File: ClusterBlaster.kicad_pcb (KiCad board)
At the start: 2 copper layers, 12 parts, among them J1 Conn_01x04, U1 LM339, U2 L7805

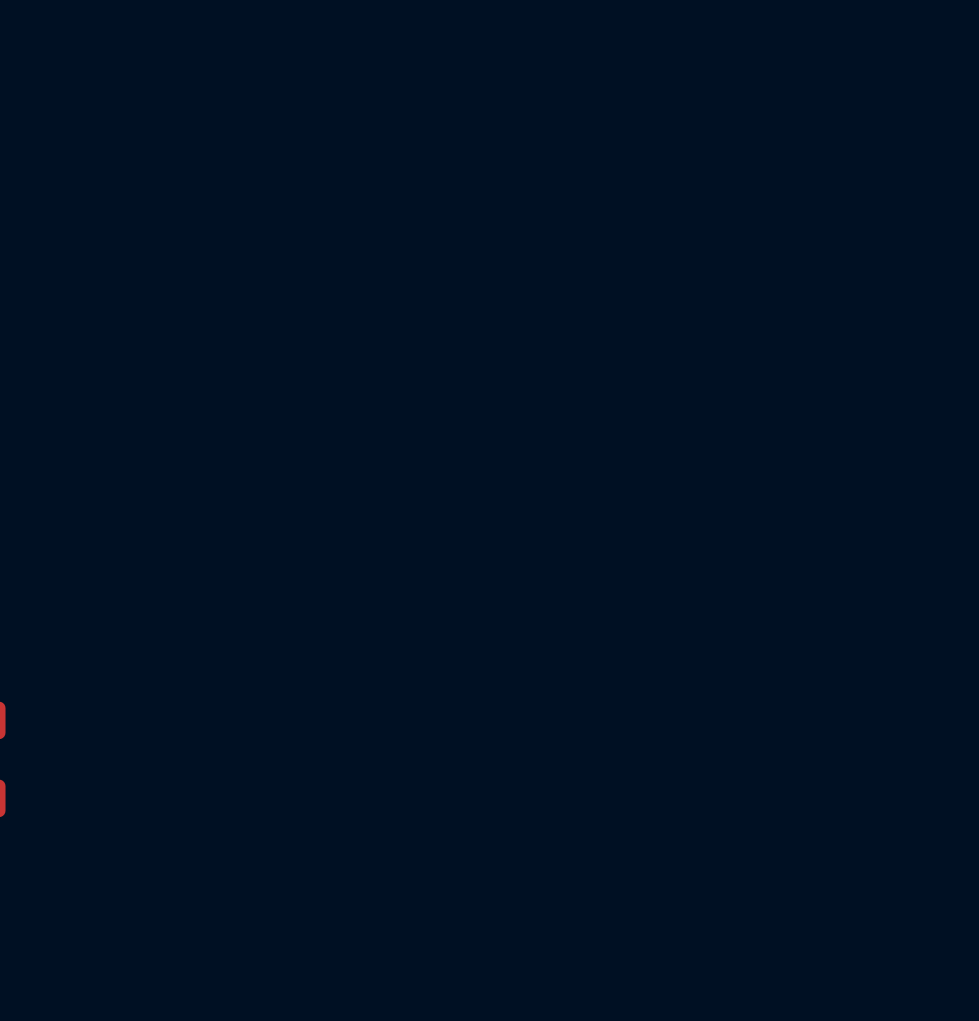
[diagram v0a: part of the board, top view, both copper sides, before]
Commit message: Added Arduino symbol and footprint
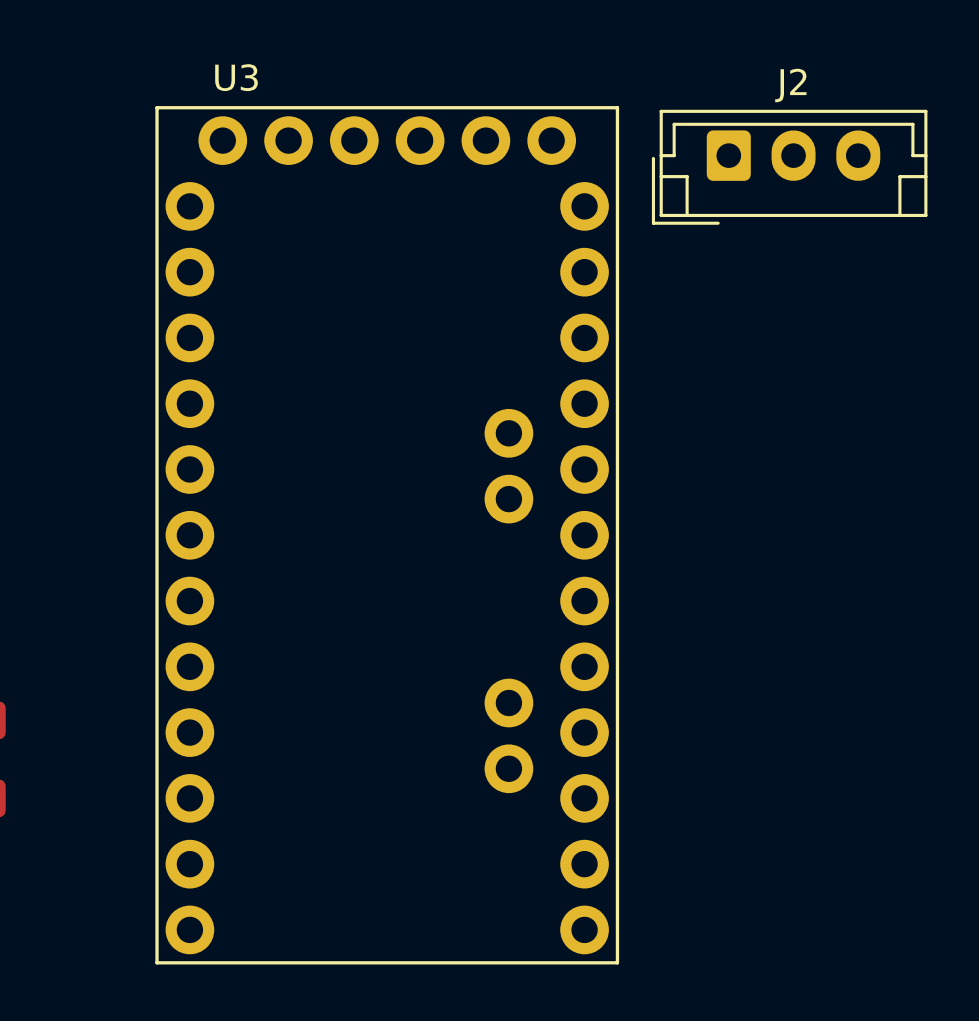
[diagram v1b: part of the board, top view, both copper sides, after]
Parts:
- added J2: Conn_01x03, Connector_JST:JST_EH_B3B-EH-A_1x03_P2.50mm_Vertical, F.Cu at (165.6, 56.5)
- added U3: ARDUINO_PRO_MINI, Pro_Mini:MODULE_ARDUINO_PRO_MINI, F.Cu at (152.4, 71.1)

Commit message: Added all the components
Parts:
- added R10: 10k, Resistor_SMD:R_0805_2012Metric, F.Cu at (175.1, 69.1)
- added R8: 10k, Resistor_SMD:R_0805_2012Metric, F.Cu at (175.1, 63.2)
- added R9: 10k, Resistor_SMD:R_0805_2012Metric, F.Cu at (175.1, 66.2)
- added SW1: SW_Push, Button_Switch_THT:SW_PUSH_6mm, F.Cu at (164.4, 63.8)
- added SW2: SW_Push, Button_Switch_THT:SW_PUSH_6mm, F.Cu at (164.4, 72.3)
- added SW3: SW_Push, Button_Switch_THT:SW_PUSH_6mm, F.Cu at (164.4, 80.9)
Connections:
- U3 pad JP1_4: unconnected-(U3-VCC-PadJP1_4) -> 5V
- U3 pad JP1_5: Net-(U3-GND-PadJP1_5) -> GND
- U3 pad JP1_6: Net-(U3-GND-PadJP1_5) -> GND
- U3 pad JP6_2: unconnected-(U3-GND_1-PadJP6_2) -> GND
- U3 pad JP6_4: unconnected-(U3-VCC_1-PadJP6_4) -> 5V
- U3 pad JP7_1: unconnected-(U3-D9-PadJP7_1) -> BTN-UP
- U3 pad JP7_2: unconnected-(U3-D8-PadJP7_2) -> BTN-DOWN
- U3 pad JP7_3: unconnected-(U3-D7-PadJP7_3) -> BTN-ENTER
- U3 pad JP7_4: unconnected-(U3-D6-PadJP7_4) -> ENABLE
- U3 pad JP7_5: unconnected-(U3-D5-PadJP7_5) -> DATA
- U3 pad JP7_6: unconnected-(U3-D4-PadJP7_6) -> CLOCK
- U3 pad JP7_7: unconnected-(U3-D3-PadJP7_7) -> TX
- U3 pad JP7_8: unconnected-(U3-D2-PadJP7_8) -> RX
- U3 pad JP7_9: unconnected-(U3-GND_2-PadJP7_9) -> GND

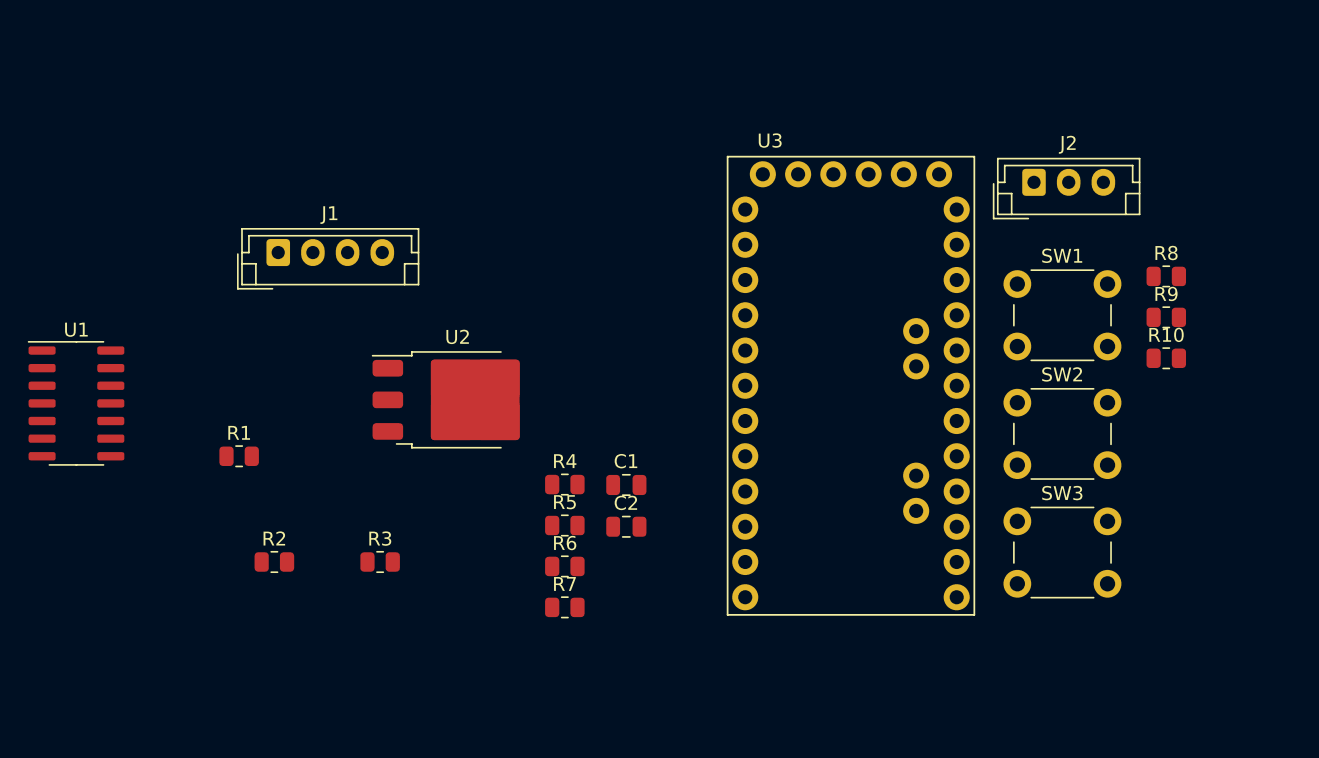
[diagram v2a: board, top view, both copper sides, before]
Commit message: Started work on PCB layout
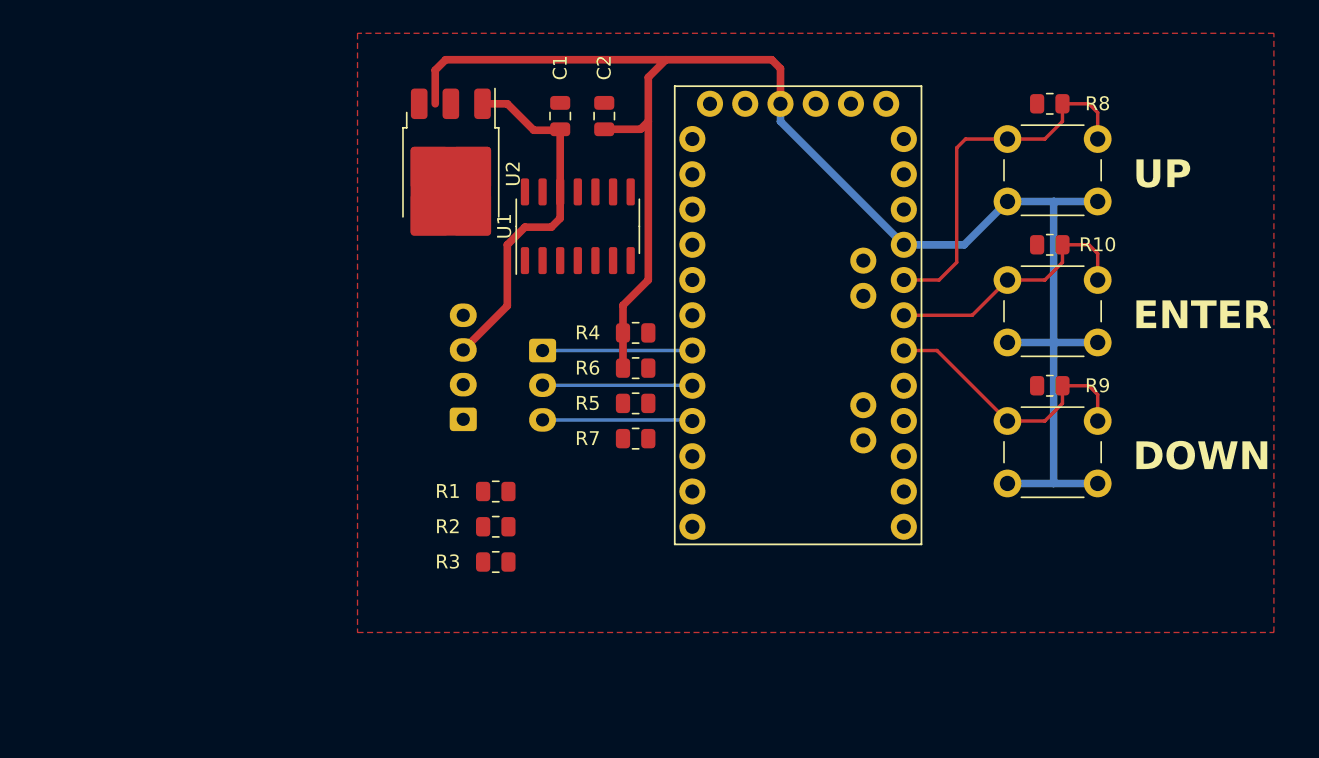
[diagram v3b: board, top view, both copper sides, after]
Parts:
- J1: value Conn_01x04 -> OBD2; moved to B.Cu
- J2: value Conn_01x03 -> Cluster; moved to B.Cu
- SW1: value SW_Push -> UP
- SW2: value SW_Push -> DOWN
- SW3: value SW_Push -> ENTER
- moved U1 38.3 mm to (132.7, 59.6), turned to 90 degrees
- moved J2 37.4 mm to (130.2, 68.6), turned to -90 degrees
- moved C2 29.6 mm to (134.6, 51.7), turned to 90 degrees
- moved C1 27.0 mm to (131.4, 51.7), turned to 90 degrees
- moved R1 18.7 mm to (126.8, 78.7)
- moved J1 18.0 mm to (124.5, 73.5), turned to 90 degrees
- moved SW3 17.4 mm to (163.7, 63.5)
- moved U2 16.3 mm to (123.6, 55.8), turned to -90 degrees
- moved R2 16.2 mm to (126.8, 81.3)
- moved R6 15.2 mm to (136.9, 69.8)
- moved R8 15.0 mm to (166.7, 50.8)
- moved R7 13.2 mm to (136.9, 74.9)
- moved R4 12.1 mm to (136.9, 67.3)
- moved R10 11.7 mm to (166.7, 61.0)
- moved SW1 10.5 mm to (163.7, 53.3)
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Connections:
- U3 pad JP6_5: unconnected-(U3-A3-PadJP6_5) -> BTN-UP
- U3 pad JP6_6: unconnected-(U3-A2-PadJP6_6) -> BTN-ENTER
- U3 pad JP6_7: unconnected-(U3-A1-PadJP6_7) -> BTN-DOWN
- U3 pad JP7_1: BTN-UP -> unconnected-(U3-D9-PadJP7_1)
- U3 pad JP7_2: BTN-DOWN -> unconnected-(U3-D8-PadJP7_2)
- U3 pad JP7_3: BTN-ENTER -> unconnected-(U3-D7-PadJP7_3)
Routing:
- net 5V: track 0.00 -> 119.8 mm
- net BTN-UP: track 0.00 -> 27.0 mm
- net +12V: track 0.00 -> 26.3 mm
- net BTN-DOWN: track 0.00 -> 20.0 mm
- net BTN-ENTER: track 0.00 -> 19.0 mm
- net ENABLE: track 0.00 -> 10.8 mm
- net DATA: track 0.00 -> 10.8 mm
- net CLOCK: track 0.00 -> 10.8 mm
- added copper zone on F.Cu, net GND

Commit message: Switched Arduino to SMD sockets
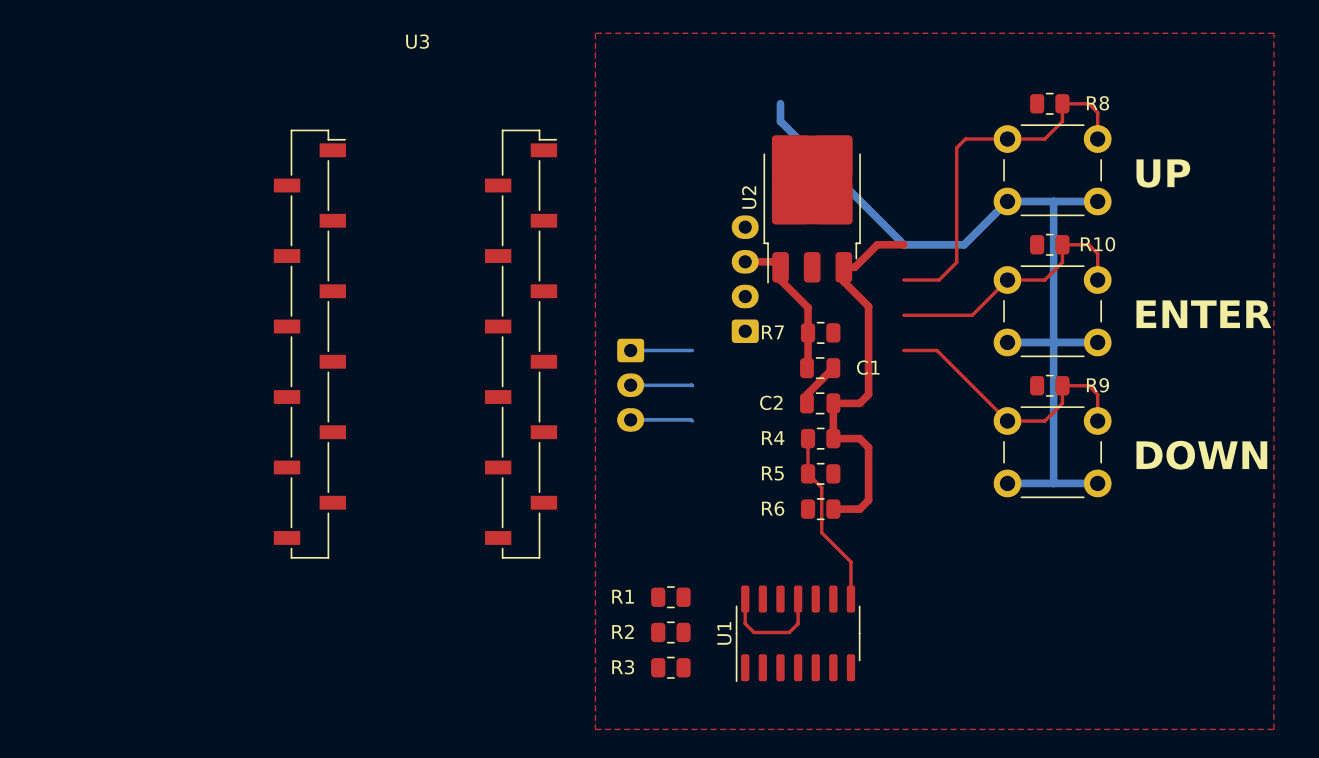
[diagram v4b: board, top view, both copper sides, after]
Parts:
- U3: footprint Pro_Mini:MODULE_ARDUINO_PRO_MINI -> Arduino Pro Mini:SMD
- moved U1 33.4 mm to (148.6, 89.0)
- moved U3 27.4 mm to (121.2, 66.0)
- moved U2 26.1 mm to (149.6, 57.5), turned to 90 degrees
- moved C1 26.1 mm to (150.2, 69.8), turned to 0 degrees
- moved C2 25.9 mm to (150.2, 72.4), turned to 180 degrees
- moved J1 21.3 mm to (144.8, 67.2)
- moved R6 16.8 mm to (150.2, 80.0), turned to 180 degrees
- moved R4 15.4 mm to (150.2, 74.9), turned to 180 degrees
- moved R7 15.4 mm to (150.2, 67.3)
- moved R1 14.7 mm to (139.4, 86.4)
- moved R2 14.7 mm to (139.4, 88.9)
- moved R3 14.7 mm to (139.4, 91.4)
- moved R5 14.3 mm to (150.2, 77.5)
- moved J2 6.35 mm to (136.5, 68.6)
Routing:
- net 5V: track 119.8 -> 92.1 mm
- net +12V: track 26.3 -> 10.8 mm
- net Net-(U1B--): track 0.00 -> 12.8 mm
- net K-Line: track 0.00 -> 7.89 mm
- net ENABLE: track 10.8 -> 4.48 mm
- net DATA: track 10.8 -> 4.46 mm
- net CLOCK: track 10.8 -> 4.44 mm
- net GND: track 0.00 -> 3.33 mm

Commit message: Routed PCB
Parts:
- J1: footprint Connector_JST:JST_EH_B4B-EH-A_1x04_P2.50mm_Vertical -> Connector_JST:JST_XH_B3B-XH-A_1x03_P2.50mm_Vertical; moved to F.Cu
- J2: value Cluster -> Cluster Display; footprint Connector_JST:JST_EH_B3B-EH-A_1x03_P2.50mm_Vertical -> Connector_JST:JST_XH_B3B-XH-A_1x03_P2.50mm_Vertical; moved to F.Cu
- SW1, SW2, SW3: moved to B.Cu
- U3: value ARDUINO_PRO_MINI -> Arduino
- moved R2 32.0 mm to (160.4, 64.8), turned to 180 degrees
- moved R1 32.0 mm to (160.4, 62.2)
- moved J2 31.5 mm to (159.4, 90.2), turned to 0 degrees
- moved R3 27.1 mm to (154.9, 69.2), turned to -90 degrees
- moved U3 21.4 mm to (135.7, 81.7), turned to 90 degrees
- moved U1 20.8 mm to (161.3, 72.5)
- moved R5 20.7 mm to (164.2, 62.2)
- moved SW2 18.1 mm to (177.8, 85.0), turned to 180 degrees
- moved R4 17.3 mm to (164.2, 64.8)
- moved C2 15.8 mm to (154.4, 57.1), turned to 90 degrees
- moved R7 15.1 mm to (158.5, 80.0)
- moved SW3 15.0 mm to (177.8, 68.5), turned to 180 degrees
- moved R9 14.3 mm to (176.9, 81.2)
- moved SW1 14.2 mm to (177.8, 52.1), turned to 180 degrees
- moved C1 13.8 mm to (144.8, 57.1), turned to 90 degrees
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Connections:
- J1 pad 1: K-Line 2 -> K-Line
- J1 pad 2: K-Line -> +12V
- J1 pad 3: +12V -> GND
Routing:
- net RX: track 0.00 -> 75.6 mm, vias 0 -> 3
- net +12V: track 10.8 -> 72.5 mm, vias 0 -> 2
- net TX: track 0.00 -> 50.0 mm, vias 0 -> 2
- net 5V: track 92.1 -> 139.3 mm, vias 0 -> 2
- net BTN-UP: track 27.0 -> 72.8 mm
- net BTN-ENTER: track 19.0 -> 60.7 mm, vias 0 -> 1
- net BTN-DOWN: track 20.0 -> 50.9 mm
- net K-Line: track 7.89 -> 34.6 mm
- net CLOCK: track 4.44 -> 25.9 mm
- net DATA: track 4.46 -> 25.6 mm
- net ENABLE: track 4.48 -> 24.8 mm
- net Net-(U1A--): track 0.16 -> 13.8 mm
- net Net-(U1A-+): track 0.00 -> 13.4 mm
- net Net-(U1B--): track 12.8 -> 20.1 mm
- net GND: track 3.33 -> 0.00 mm, vias 0 -> 8
- added copper zone on B.Cu, net GND
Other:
- board outline added: 65.4 x 50.2 mm

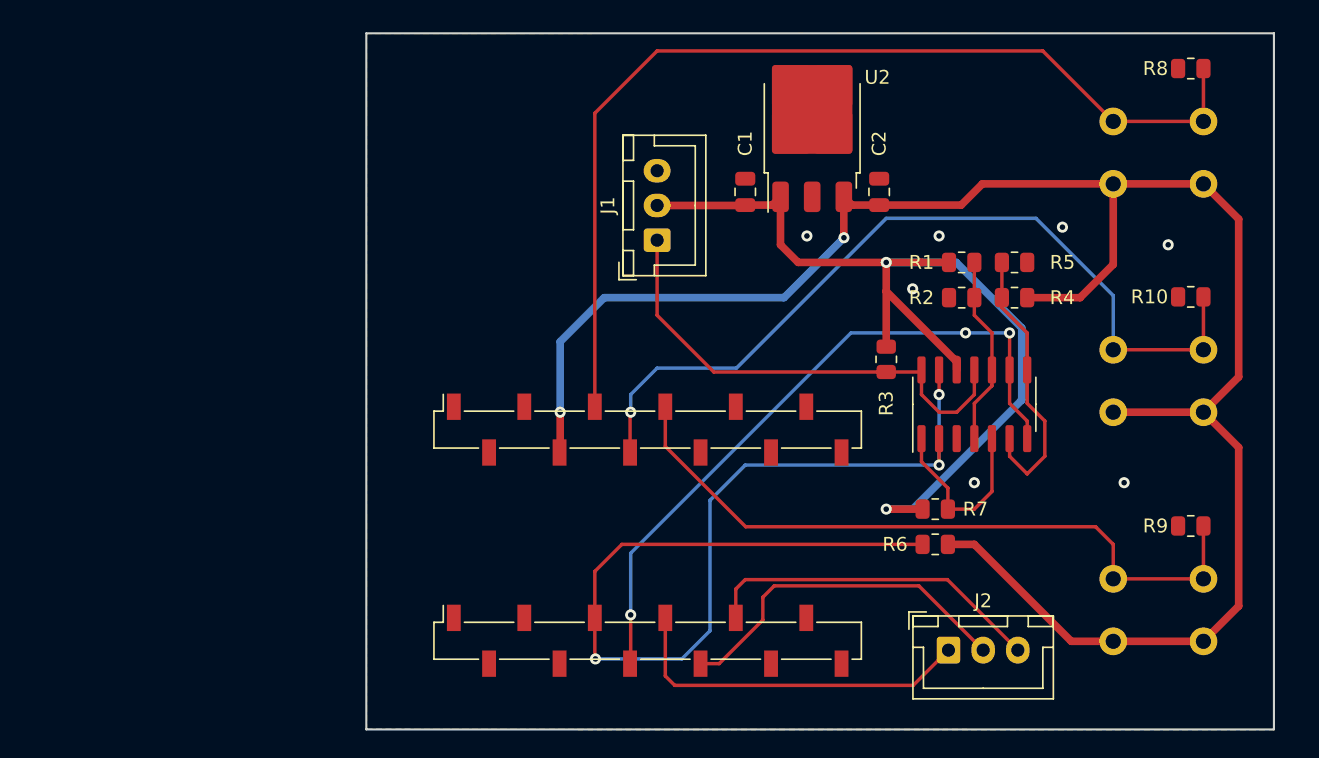
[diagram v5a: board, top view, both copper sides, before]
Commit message: Added logo and revision
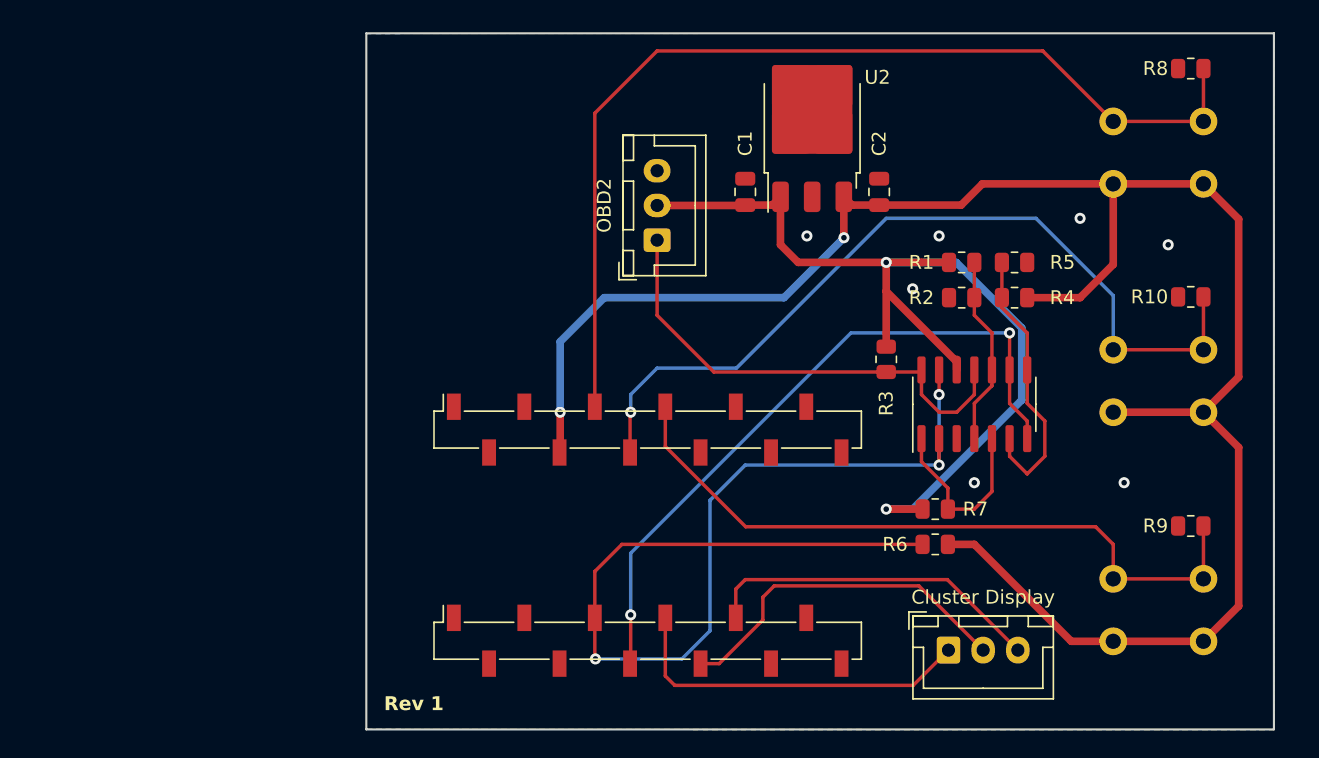
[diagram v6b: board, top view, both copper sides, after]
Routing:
- net GND: vias 8 -> 7
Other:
- board text added: "Rev 1"

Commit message: Made the schematic cleaner
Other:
- board text added: "Rev: 1"
- board text removed: "Rev 1"
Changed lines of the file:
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@@
   (gr_rect (start 117.475 45.72) (end 182.88 95.885)
     (stroke (width 0.15) (type default)) (fill none) (layer "Edge.Cuts"))
-  (gr_text "Rev 1" (at 118.745 94.615) (layer "F.SilkS")
+  (gr_text "Rev: 1" (at 118.745 94.615) (layer "F.SilkS")
     (effects (font (size 1 1) (thickness 0.25) bold) (justify left bottom))
   )
